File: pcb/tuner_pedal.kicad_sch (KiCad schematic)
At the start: 16 parts, among them U1 STM32F411CEUx, U2 PCM1802DB, X1 ECS-2520MVLC-081.92

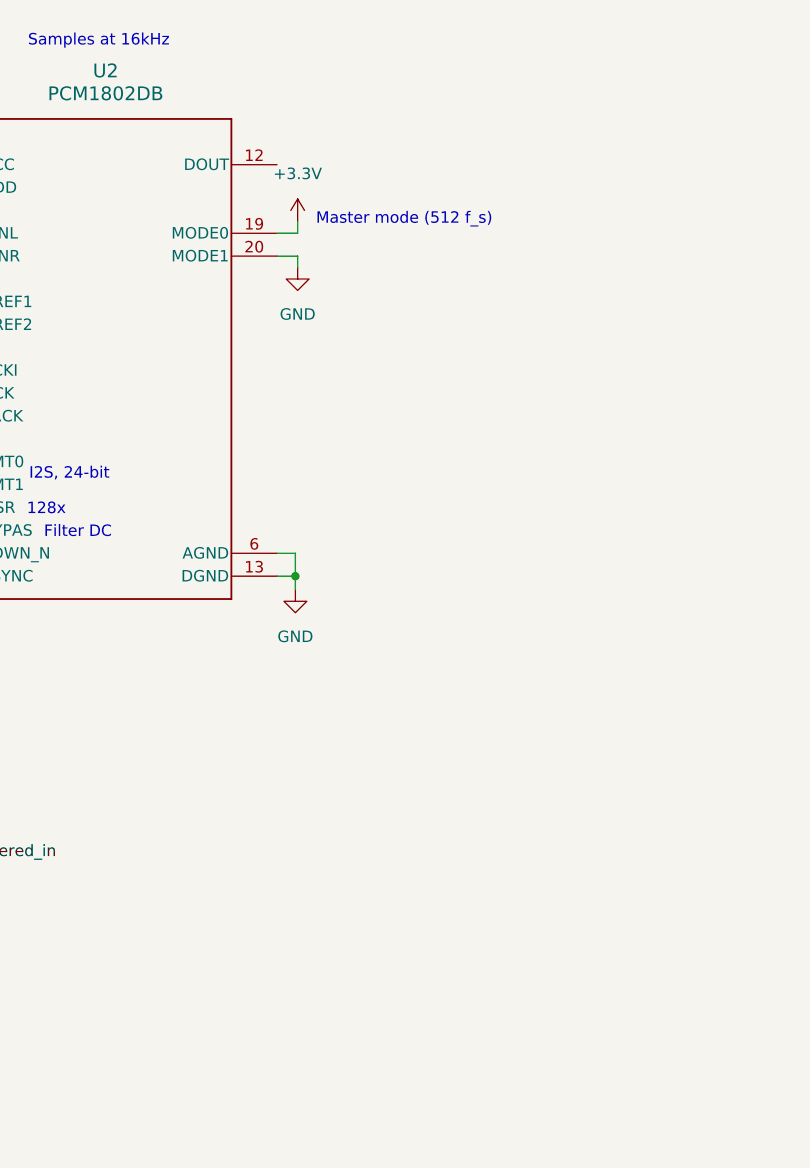
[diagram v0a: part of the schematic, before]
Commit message: Added 5->3.3V LDO
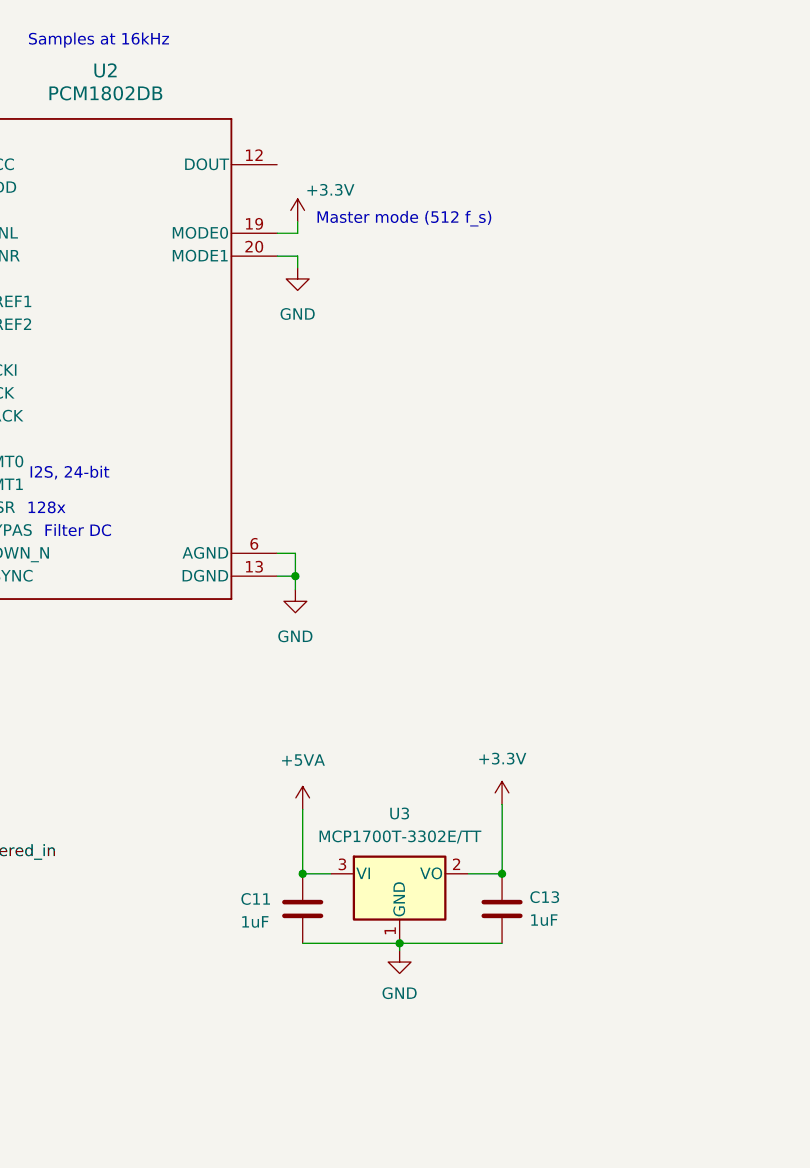
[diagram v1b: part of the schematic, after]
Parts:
- added C11, C13: 1uF, symbol Device:C
- added U3: MCP1700T-3302E/TT, Package_TO_SOT_SMD:SOT-23-3, symbol Regulator_Linear:MCP1700x-330xxTT
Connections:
- net +3.3V: now also C13.1, U3.2 (VO)
- net +5VA: now also C11.1, U3.3 (VI)
- net GND: now also C11.2, C13.2, U3.1 (GND)
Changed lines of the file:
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@@
   (junction (at 24.511 58.674) (diameter 0) (color 0 0 0 0)
   )
+  (junction (at 97.0788 122.2248) (diameter 0) (color 0 0 0 0)
+  )
   (junction (at 50.546 84.074) (diameter 0) (color 0 0 0 0)
   )
@@
   (junction (at 38.608 70.866) (diameter 0) (color 0 0 0 0)
   )
+  (junction (at 119.2276 122.2248) (diameter 0) (color 0 0 0 0)
+  )
   (junction (at 29.972 70.866) (diameter 0) (color 0 0 0 0)
   )
@@
   (junction (at 23.622 41.656) (diameter 0) (color 0 0 0 0)
   )
+  (junction (at 107.8484 129.9464) (diameter 0) (color 0 0 0 0)
+  )
   (junction (at 28.702 41.656) (diameter 0) (color 0 0 0 0)
   )
@@
     (stroke (width 0) (type default))
   )
+  (wire (pts (xy 107.8484 129.9464) (xy 107.8484 130.7592))
+    (stroke (width 0) (type default))
+  )
   (wire (pts (xy 44.196 61.214) (xy 44.196 70.866))
     (stroke (width 0) (type default))
@@
     (stroke (width 0) (type default))
   )
+  (wire (pts (xy 97.0788 122.2248) (xy 97.0788 122.3264))
+    (stroke (width 0) (type default))
+  )
   (wire (pts (xy 45.212 24.13) (xy 45.212 29.21))
     (stroke (width 0) (type default))
@@
     (stroke (width 0) (type default))
   )
+  (wire (pts (xy 119.2276 114.5032) (xy 119.2276 122.2248))
+    (stroke (width 0) (type default))
+  )
+  (wire (pts (xy 97.0788 115.062) (xy 97.0788 122.2248))
+    (stroke (width 0) (type default))
+  )
   (wire (pts (xy 96.266 89.154) (xy 96.266 90.678))
     (stroke (width 0) (type default))
@@
     (stroke (width 0) (type default))
   )
+  (wire (pts (xy 107.8484 129.8448) (xy 107.8484 129.9464))
+    (stroke (width 0) (type default))
+  )
   (wire (pts (xy 56.134 89.154) (xy 50.546 89.154))
     (stroke (width 0) (type default))
@@
     (stroke (width 0) (type default))
   )
+  (wire (pts (xy 107.8484 129.9464) (xy 119.2276 129.9464))
+    (stroke (width 0) (type default))
+  )
   (wire (pts (xy 29.972 68.834) (xy 29.972 70.866))
     (stroke (width 0) (type default))
@@
     (stroke (width 0) (type default))
   )
+  (wire (pts (xy 119.2276 122.2248) (xy 119.2276 122.3264))
+    (stroke (width 0) (type default))
+  )
   (wire (pts (xy 96.52 53.594) (xy 96.52 54.864))
     (stroke (width 0) (type default))
@@
     (stroke (width 0) (type default))
   )
+  (wire (pts (xy 97.0788 129.9464) (xy 107.8484 129.9464))
+    (stroke (width 0) (type default))
+  )
   (wire (pts (xy 52.1208 66.294) (xy 56.134 66.294))
     (stroke (width 0) (type default))
@@
     (stroke (width 0) (type default))
   )
+  (wire (pts (xy 115.4684 122.2248) (xy 119.2276 122.2248))
+    (stroke (width 0) (type default))
+  )
   (wire (pts (xy 39.4208 51.1048) (xy 56.134 51.054))
     (stroke (width 0) (type default))
@@
   )
   (wire (pts (xy 47.625 76.454) (xy 47.625 81.534))
+    (stroke (width 0) (type default))
+  )
+  (wire (pts (xy 100.2284 122.2248) (xy 97.0788 122.2248))
     (stroke (width 0) (type default))
   )
@@
     (effects (font (size 1.27 1.27)) (justify left bottom))
   )
+  (symbol (lib_id "power:+5VA") (at 97.0788 115.062 0) (unit 1)
+    (in_bom yes) (on_board yes) (dnp no) (fields_autoplaced)
+    (property "Reference" "#PWR011" (at 97.0788 118.872 0)
+      (effects (font (size 1.27 1.27)) hide)
+    )
+    (property "Value" "+5VA" (at 97.0788 109.6264 0)
+      (effects (font (size 1.27 1.27)))
+    )
+    (property "Footprint" "" (at 97.0788 115.062 0)
+      (effects (font (size 1.27 1.27)) hide)
+    )
+    (property "Datasheet" "" (at 97.0788 115.062 0)
+      (effects (font (size 1.27 1.27)) hide)
+    )
+    (pin "1")
+    (instances
+      (project "tuner_pedal"
+        (path "/be09f3cc-c79c-49de-93a4-4a01bf6bfbcf"
+          (reference "#PWR011") (unit 1)
+        )
+      )
+    )
+  )
   (symbol (lib_id "power:+3.3V") (at 46.6852 153.4668 0) (unit 1)
     (in_bom yes) (on_board yes) (dnp no)
@@
   )
   (symbol (lib_id "power:+3.3V") (at 96.52 49.784 0) (unit 1)
-    (in_bom yes) (on_board yes) (dnp no) (fields_autoplaced)
+    (in_bom yes) (on_board yes) (dnp no)
     (property "Reference" "#PWR014" (at 96.52 53.594 0)
       (effects (font (size 1.27 1.27)) hide)
     )
-    (property "Value" "+3.3V" (at 96.52 44.45 0)
+    (property "Value" "+3.3V" (at 100.1268 46.2788 0)
       (effects (font (size 1.27 1.27)))
     )
@@
         (path "/be09f3cc-c79c-49de-93a4-4a01bf6bfbcf"
           (reference "#PWR02") (unit 1)
+        )
+      )
+    )
+  )
+  (symbol (lib_id "power:+3.3V") (at 119.2276 114.5032 0) (unit 1)
+    (in_bom yes) (on_board yes) (dnp no) (fields_autoplaced)
+    (property "Reference" "#PWR012" (at 119.2276 118.3132 0)
+      (effects (font (size 1.27 1.27)) hide)
+    )
+    (property "Value" "+3.3V" (at 119.2276 109.474 0)
+      (effects (font (size 1.27 1.27)))
+    )
+    (property "Footprint" "" (at 119.2276 114.5032 0)
+      (effects (font (size 1.27 1.27)) hide)
+    )
+    (property "Datasheet" "" (at 119.2276 114.5032 0)
+      (effects (font (size 1.27 1.27)) hide)
+    )
+    (pin "1")
+    (instances
+      (project "tuner_pedal"
+        (path "/be09f3cc-c79c-49de-93a4-4a01bf6bfbcf"
+          (reference "#PWR012") (unit 1)
         )
       )
@@
     )
   )
+  (symbol (lib_id "Device:C") (at 97.0788 126.1364 0) (unit 1)
+    (in_bom yes) (on_board yes) (dnp no)
+    (property "Reference" "C11" (at 90.17 125.0696 0)
+      (effects (font (size 1.27 1.27)) (justify left))
+    )
+    (property "Value" "1uF" (at 90.17 127.6096 0)
+      (effects (font (size 1.27 1.27)) (justify left))
+    )
+    (property "Footprint" "" (at 98.044 129.9464 0)
+      (effects (font (size 1.27 1.27)) hide)
+    )
+    (property "Datasheet" "~" (at 97.0788 126.1364 0)
+      (effects (font (size 1.27 1.27)) hide)
+    )
+    (pin "1")
+    (pin "2")
+    (instances
+      (project "tuner_pedal"
+        (path "/be09f3cc-c79c-49de-93a4-4a01bf6bfbcf"
+          (reference "C11") (unit 1)
+        )
+      )
+    )
+  )
   (symbol (lib_id "pcm1802:PCM1802DB") (at 56.134 43.434 0) (unit 1)
     (in_bom yes) (on_board yes) (dnp no) (fields_autoplaced)
@@
     )
   )
+  (symbol (lib_id "Regulator_Linear:MCP1700x-330xxTT") (at 107.8484 122.2248 0) (unit 1)
+    (in_bom yes) (on_board yes) (dnp no) (fields_autoplaced)
+    (property "Reference" "U3" (at 107.8484 115.57 0)
+      (effects (font (size 1.27 1.27)))
+    )
+    (property "Value" "MCP1700T-3302E/TT" (at 107.8484 118.11 0)
+      (effects (font (size 1.27 1.27)))
+    )
+    (property "Footprint" "Package_TO_SOT_SMD:SOT-23-3" (at 107.8484 116.5098 0)
+      (effects (font (size 1.27 1.27)) hide)
+    )
+    (property "Datasheet" "http://ww1.microchip.com/downloads/en/DeviceDoc/20001826D.pdf" (at 107.8484 122.2248 0)
+      (effects (font (size 1.27 1.27)) hide)
+    )
+    (pin "1")
+    (pin "2")
+    (pin "3")
+    (instances
+      (project "tuner_pedal"
+        (path "/be09f3cc-c79c-49de-93a4-4a01bf6bfbcf"
+          (reference "U3") (unit 1)
+        )
+      )
+    )
+  )
   (symbol (lib_id "power:+3.3V") (at 47.625 74.168 0) (unit 1)
     (in_bom yes) (on_board yes) (dnp no)
@@
         (path "/be09f3cc-c79c-49de-93a4-4a01bf6bfbcf"
           (reference "#PWR016") (unit 1)
+        )
+      )
+    )
+  )
+  (symbol (lib_id "power:GND") (at 107.8484 130.7592 0) (unit 1)
+    (in_bom yes) (on_board yes) (dnp no) (fields_autoplaced)
+    (property "Reference" "#PWR013" (at 107.8484 137.1092 0)
+      (effects (font (size 1.27 1.27)) hide)
+    )
+    (property "Value" "GND" (at 107.8484 135.5344 0)
+      (effects (font (size 1.27 1.27)))
+    )
+    (property "Footprint" "" (at 107.8484 130.7592 0)
+      (effects (font (size 1.27 1.27)) hide)
+    )
+    (property "Datasheet" "" (at 107.8484 130.7592 0)
+      (effects (font (size 1.27 1.27)) hide)
+    )
+    (pin "1")
+    (instances
+      (project "tuner_pedal"
+        (path "/be09f3cc-c79c-49de-93a4-4a01bf6bfbcf"
+          (reference "#PWR013") (unit 1)
         )
       )
@@
         )
       )
+    )
+  )
+  (symbol (lib_id "Device:C") (at 119.2276 126.1364 0) (unit 1)
+    (in_bom yes) (on_board yes) (dnp no) (fields_autoplaced)
+    (property "Reference" "C13" (at 122.2756 124.8664 0)
+      (effects (font (size 1.27 1.27)) (justify left))
+    )
+    (property "Value" "1uF" (at 122.2756 127.4064 0)
+      (effects (font (size 1.27 1.27)) (justify left))
+    )
+    (property "Footprint" "" (at 120.1928 129.9464 0)
+      (effects (font (size 1.27 1.27)) hide)
+    )
+    (property "Datasheet" "~" (at 119.2276 126.1364 0)
+      (effects (font (size 1.27 1.27)) hide)
+    )
+    (pin "1")
+    (pin "2")
+    (instances
+      (project "tuner_pedal"
+        (path "/be09f3cc-c79c-49de-93a4-4a01bf6bfbcf"
+          (reference "C13") (unit 1)
+        )
+      )

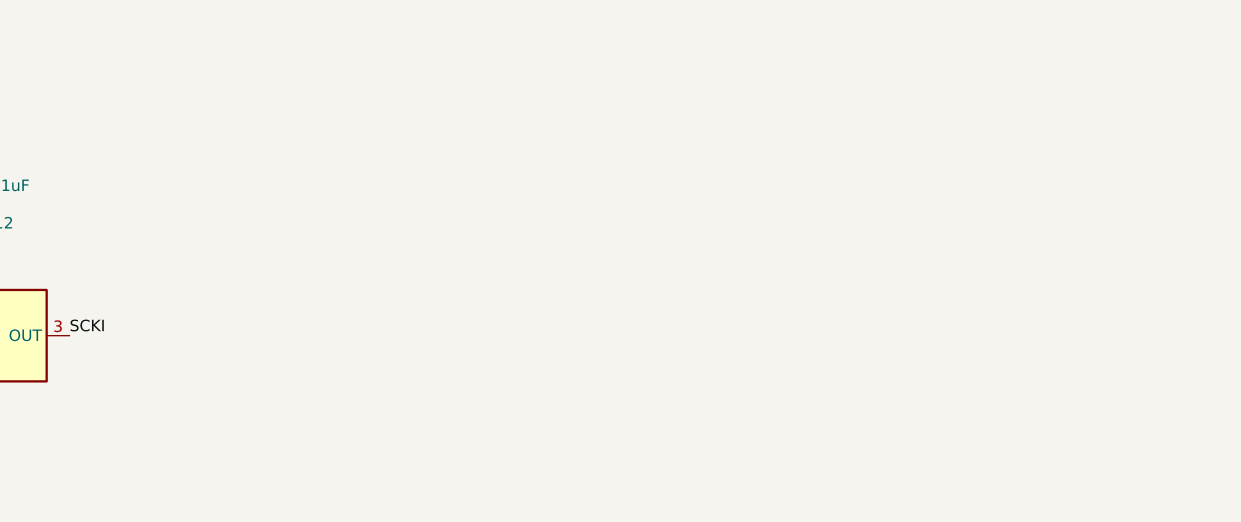
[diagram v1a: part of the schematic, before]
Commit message: Added 9V->5V buck converter
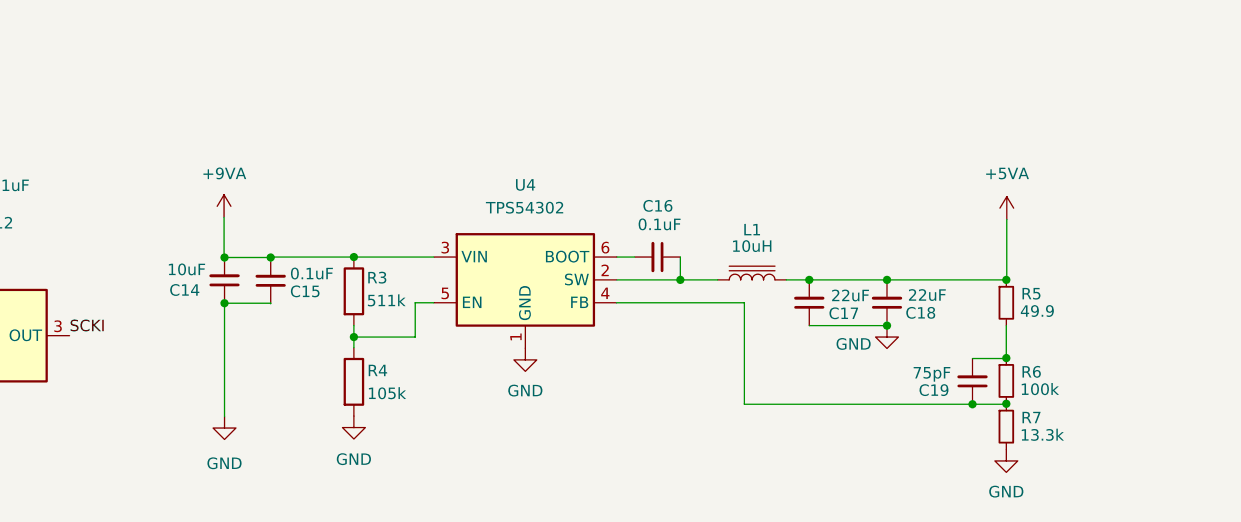
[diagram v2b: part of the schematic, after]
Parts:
- added C14: 10uF, symbol Device:C_Small
- added C15, C16: 0.1uF, symbol Device:C_Small
- added C17, C18: 22uF, symbol Device:C_Small
- added C19: 75pF, symbol Device:C_Small
- added L1: 10uH, symbol Device:L_Iron
- added R3: 511k, symbol Device:R
- added R4: 105k, symbol Device:R
- added R5: 49.9, symbol Device:R_Small
- added R6: 100k, symbol Device:R_Small
- added R7: 13.3k, symbol Device:R_Small
- added U4: TPS54302, Package_TO_SOT_SMD:SOT-23-6, symbol Regulator_Switching:TPS54302
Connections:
- net +5VA: now also C17.2, C18.2, L1.2, R5.1
- net GND: now also C14.1, C15.1, C17.1, C18.1, R4.2, R7.2, U4.1 (GND)
- new net: C16.1, L1.1, U4.2 (SW)
- new net: C16.2, U4.6 (BOOT)
- new net: C19.1, R6.2, R7.1, U4.4 (FB)
- new net: C19.2, R5.2, R6.1
- new net: R3.2, R4.1, U4.5 (EN)
- new net +9VA: C14.2, C15.2, R3.1, U4.3 (VIN)

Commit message: added AC coupling cap to unused V_inR
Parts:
- added C20: 1uF, symbol Device:C_Polarized_Small_US
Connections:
- net GND: now also C20.2; no longer U2.2 (VINR)
- new net: C20.1, U2.2 (VINR)
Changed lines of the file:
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@@
   (junction (at 42.418 41.656) (diameter 0) (color 0 0 0 0)
   )
+  (junction (at 19.4056 53.594) (diameter 0) (color 0 0 0 0)
+  )
   (junction (at 24.892 70.866) (diameter 0) (color 0 0 0 0)
   )
@@
   (junction (at 45.212 29.21) (diameter 0) (color 0 0 0 0)
   )
-  (junction (at 19.431 53.594) (diameter 0) (color 0 0 0 0)
-  )
   (junction (at 19.431 41.656) (diameter 0) (color 0 0 0 0)
   )
@@
     (stroke (width 0) (type default))
   )
+  (wire (pts (xy 19.4056 53.594) (xy 19.4056 58.674))
+    (stroke (width 0) (type default))
+  )
   (wire (pts (xy 97.3328 165.4556) (xy 88.4428 165.4556))
     (stroke (width 0) (type default))
@@
     (stroke (width 0) (type default))
   )
+  (wire (pts (xy 19.4056 41.656) (xy 19.431 41.656))
+    (stroke (width 0) (type default))
+  )
   (wire (pts (xy 29.591 58.674) (xy 29.591 60.452))
     (stroke (width 0) (type default))
@@
     (stroke (width 0) (type default))
   )
-  (wire (pts (xy 19.431 53.594) (xy 19.431 58.674))
+  (wire (pts (xy 19.4056 41.656) (xy 19.4056 53.594))
+    (stroke (width 0) (type default))
+  )
+  (wire (pts (xy 19.4056 53.594) (xy 40.9956 53.594))
+    (stroke (width 0) (type default))
+  )
+  (wire (pts (xy 19.4056 58.674) (xy 19.431 58.674))
     (stroke (width 0) (type default))
   )
@@
     (stroke (width 0) (type default))
   )
+  (wire (pts (xy 46.0756 53.594) (xy 56.134 53.594))
+    (stroke (width 0) (type default))
+  )
   (wire (pts (xy 131.826 170.5356) (xy 131.826 181.8132))
     (stroke (width 0) (type default))
@@
     (stroke (width 0) (type default))
   )
-  (wire (pts (xy 19.431 53.594) (xy 56.134 53.594))
-    (stroke (width 0) (type default))
-  )
   (wire (pts (xy 88.4428 175.514) (xy 88.4428 174.3456))
     (stroke (width 0) (type default))
@@
   )
   (wire (pts (xy 50.546 84.074) (xy 50.546 89.154))
-    (stroke (width 0) (type default))
-  )
-  (wire (pts (xy 19.431 41.656) (xy 19.431 53.594))
     (stroke (width 0) (type default))
   )
@@
         )
       )
+    )
+  )
+  (symbol (lib_id "Device:C_Polarized_Small_US") (at 43.5356 53.594 270) (unit 1)
+    (in_bom yes) (on_board yes) (dnp no)
+    (property "Reference" "C20" (at 41.2496 56.3372 90)
+      (effects (font (size 1.27 1.27)))
+    )
+    (property "Value" "1uF" (at 45.8216 56.3372 90)
+      (effects (font (size 1.27 1.27)))
+    )
+    (property "Footprint" "" (at 43.5356 53.594 0)
+      (effects (font (size 1.27 1.27)) hide)
+    )
+    (property "Datasheet" "~" (at 43.5356 53.594 0)
+      (effects (font (size 1.27 1.27)) hide)
+    )
+    (pin "1")
+    (pin "2")
+    (instances
+      (project "tuner_pedal"
+        (path "/be09f3cc-c79c-49de-93a4-4a01bf6bfbcf"
+          (reference "C20") (unit 1)
+        )
+      )
